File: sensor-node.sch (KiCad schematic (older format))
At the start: 38 parts

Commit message: init
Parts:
- U? (x2): symbol PS2811-1 -> PS2811-1-RESCUE-sensor-node
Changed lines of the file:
@@
 EESchema Schematic File Version 2
+LIBS:sensor-node-rescue
 LIBS:power
 LIBS:device
@@
 $EndComp
 $Comp
-L PS2811-1 U?
+L PS2811-1-RESCUE-sensor-node U?
 U 1 1 59702874
 P 2150 3600
@@
 $EndComp
 $Comp
-L PS2811-1 U?
+L PS2811-1-RESCUE-sensor-node U?
 U 1 1 59708087
 P 2150 4250

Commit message: init
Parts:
- removed J?: CONN_01X03, symbol CONN_01X03
- added J?: GND, symbol CONN_01X01
- added J?: +24, symbol CONN_01X01
- added J?: RJ45_B, symbol CONN_02X04
- added J?: ANALOG_IN, symbol CONN_01X02
- C? (x2): value C -> 0.1uF
- C?: value C -> 10uF
- C?: value C -> 4700pF
- C? (x2): value C -> 27pF
- C?: value CP -> 100uF
- C?: value CP -> 1000uF
- J?: value CONN_01X02 -> I2C
- J?: value OUTPUT -> DIGITAL_OUT
- J?: value INPUT -> DIGITAL_IN
- J?: value RJ45 -> RJ45_A
- R? (x2): value R -> 60
- R?: value R -> 300
- R? (x2): value R -> 4.7K
- Y?: value Crystal -> 8MHz
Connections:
- net +3V3: no longer J?.1 (P1), J?.2 (P2)
- net +5V: now also J?.1 (P1), J?.2 (P2), J?.1 (P1), J?.2 (P2)
- net CANH: now also J?.7 (P7), J?.7 (P7)
- net CANL: now also J?.8 (P8), J?.8 (P8)
- net GND: now also J?.5 (P5), J?.6 (P6), J?.1 (P1), J?.2 (P2), J?.5 (P5), J?.6 (P6); no longer J?.3 (P3), J?.4 (P4), U?.4 (D), U?.4 (D)
- net at U?.6 (PA0): now also J?.1 (P1)
- net at C?.2, R?.1, R?.1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: no longer J?.7 (P7), J?.8 (P8)
- net at J?.2 (P2), U?.2 (D): now also U?.4 (D)
- net at J?.1 (P1), U?.2 (D): now also U?.4 (D)
- new net +24V: J?.1 (P1), J?.3 (P3), J?.3 (P3), J?.4 (P4), J?.4 (P4)
- no-connect marks 2 -> 0
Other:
- moved on the sheet: J?

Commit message: updates
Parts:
- removed U?: LM1117-3.3, symbol LM1117-3.3
- added D3, D4: D_Schottky, Diodes_SMD:D_0805, symbol D_Schottky
- added D5: LED, Diodes_SMD:D_0805, symbol LED
- added J12: +5, ab2_connector:AB2_0.25_QD_TAB, symbol CONN_01X01
- added J8: CORTEX_DEBUG, Pin_Headers:Pin_Header_Straight_2x05_Pitch1.27mm, symbol CONN_02X05
- added R10: 250K, Resistors_SMD:R_0805_HandSoldering, symbol R
- added R16: 1K, Resistors_SMD:R_0805_HandSoldering, symbol R
- added R17: 330, Resistors_SMD:R_0805_HandSoldering, symbol R
- added R9: 7K, Resistors_SMD:R_0805_HandSoldering, symbol R
- added U1: LM1117-3.3, TO_SOT_Packages_SMD:SOT-223, symbol LM1117-3.3
- added U7: LM321, TO_SOT_Packages_SMD:SOT-23-5, symbol LM321
- C1: renamed from C?; value 100uF -> 10uF; footprint (none) -> Capacitors_SMD:C_0805_HandSoldering
- C2: renamed from C?; value 1000uF -> 100uF; footprint (none) -> Capacitors_SMD:C_1210_HandSoldering
- C3, C4, C5, C6, C7, C8: renamed from C?; footprint (none) -> Capacitors_SMD:C_0805_HandSoldering
- D1, D2: renamed from D?; footprint (none) -> Diodes_SMD:D_0805
- J1, J10, J11, J2: renamed from J?; footprint (none) -> Connectors_Terminal_Blocks:TerminalBlock_Pheonix_MKDS1.5-2pol
- J3, J4: renamed from J?; footprint (none) -> ab2_connector:AB2_0.25_QD_TAB
- J5, J6: renamed from J?; footprint (none) -> Pin_Headers:Pin_Header_Straight_1x02_Pitch2.54mm
- J7, J9: renamed from J?; footprint (none) -> Connectors:RJ45_8
- R1, R11, R12, R13, R14, R15, R2, R3, R4, R5, R6, R7, R8: renamed from R?; footprint (none) -> Resistors_SMD:R_0805_HandSoldering
- U2, U3: renamed from U?; footprint (none) -> Housings_SSOP:SOP-4_4.4x2.8mm_Pitch1.27mm
- U4: renamed from U?; footprint (none) -> Housings_QFP:LQFP-32_7x7mm_Pitch0.8mm
- U5, U6: renamed from U?; footprint (none) -> TO_SOT_Packages_SMD:SOT-223
- Y1: renamed from Y?; footprint (none) -> Crystals:Crystal_SMD_HC49-SD_HandSoldering
- gave numbers to parts that had none: 1
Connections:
- net +24V: now also U7.5 (V+)
- net +3V3: now also D3.1 (K), J8.1 (P1), U1.2 (VO), U1.4 (VO), U7.1 (+); no longer U4.4 (NRST)
- net +5V: now also J12.1 (P1), R17.2, U1.3 (VI)
- net GND: now also D4.2 (A), D5.1 (K), J8.3 (P3), J8.5 (P5), U1.1 (GND/ADJ), U7.2 (V-)
- net SWCLK: now also J8.4 (P4)
- net SWDIO: now also J8.2 (P2)
- net at U4.6 (PA0): now also D3.2 (A), D4.1 (K), R16.2; no longer J11.1 (P1)
- new net: J11.1 (P1), R10.1
- new net: R10.2, R9.1, U7.3 (-)
- new net: R16.1, R9.2, U7.4
- new net: D5.2 (A), R17.1
- new net NRST: J8.10 (P10), U4.4 (NRST)
- no-connect marks 0 -> 17

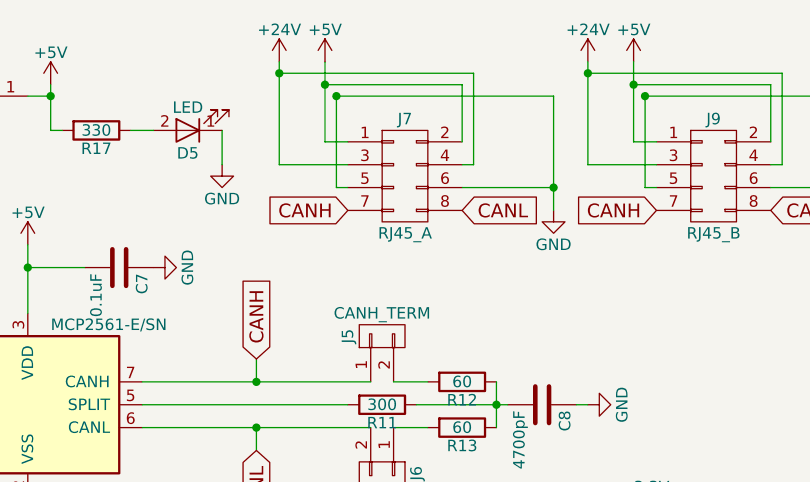
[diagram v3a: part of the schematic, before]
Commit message: Layout chaged for better routing on  the CAN differential
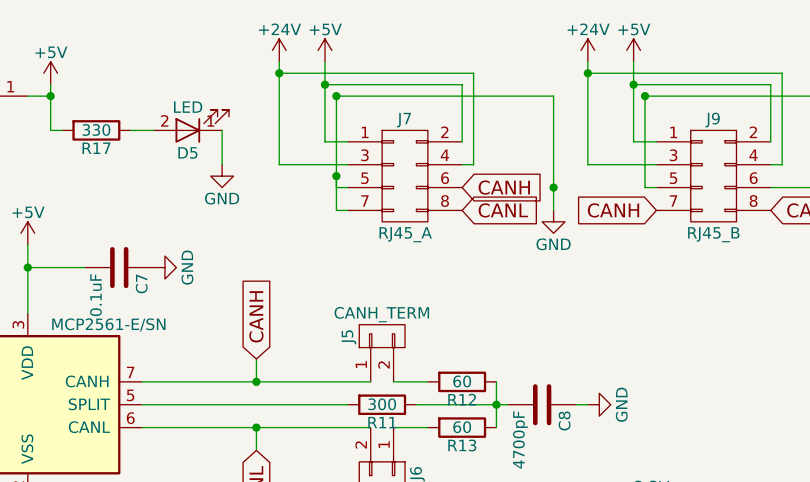
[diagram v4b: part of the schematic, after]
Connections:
- net CANH: now also J7.6 (P6); no longer J7.7 (P7)
- net GND: now also J7.7 (P7); no longer J7.6 (P6)
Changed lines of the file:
@@
 Text GLabel 8450 2000 1    60   Input ~ 0
 CANH
-Text GLabel 8850 1350 0    60   Input ~ 0
+Text GLabel 9350 1250 2    60   Input ~ 0
 CANH
 Text GLabel 9350 1350 2    60   Input ~ 0
@@
 Wire Wire Line
 	9750 1350 9750 850
-Wire Wire Line
-	9350 1250 9750 1250
 Connection ~ 9750 1250
 Wire Wire Line
@@
 Wire Wire Line
 	8300 1150 8300 1000
+Wire Wire Line
+	8850 1350 8800 1350
+Wire Wire Line
+	8800 1350 8800 1200
+Connection ~ 8800 1200
 $EndSCHEMATC

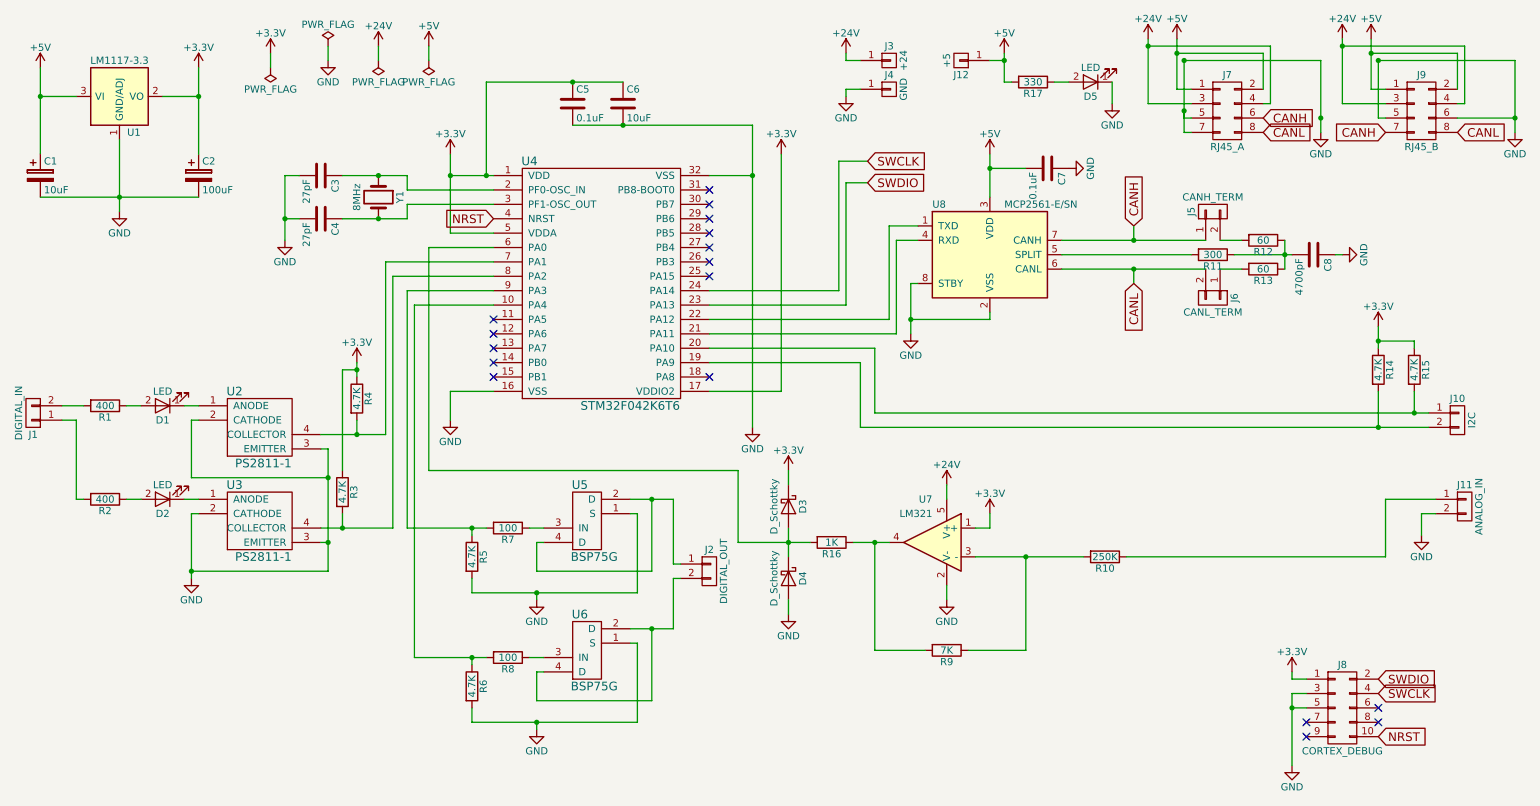
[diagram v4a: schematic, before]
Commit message: Adding voltage divider/unity gain analog front end
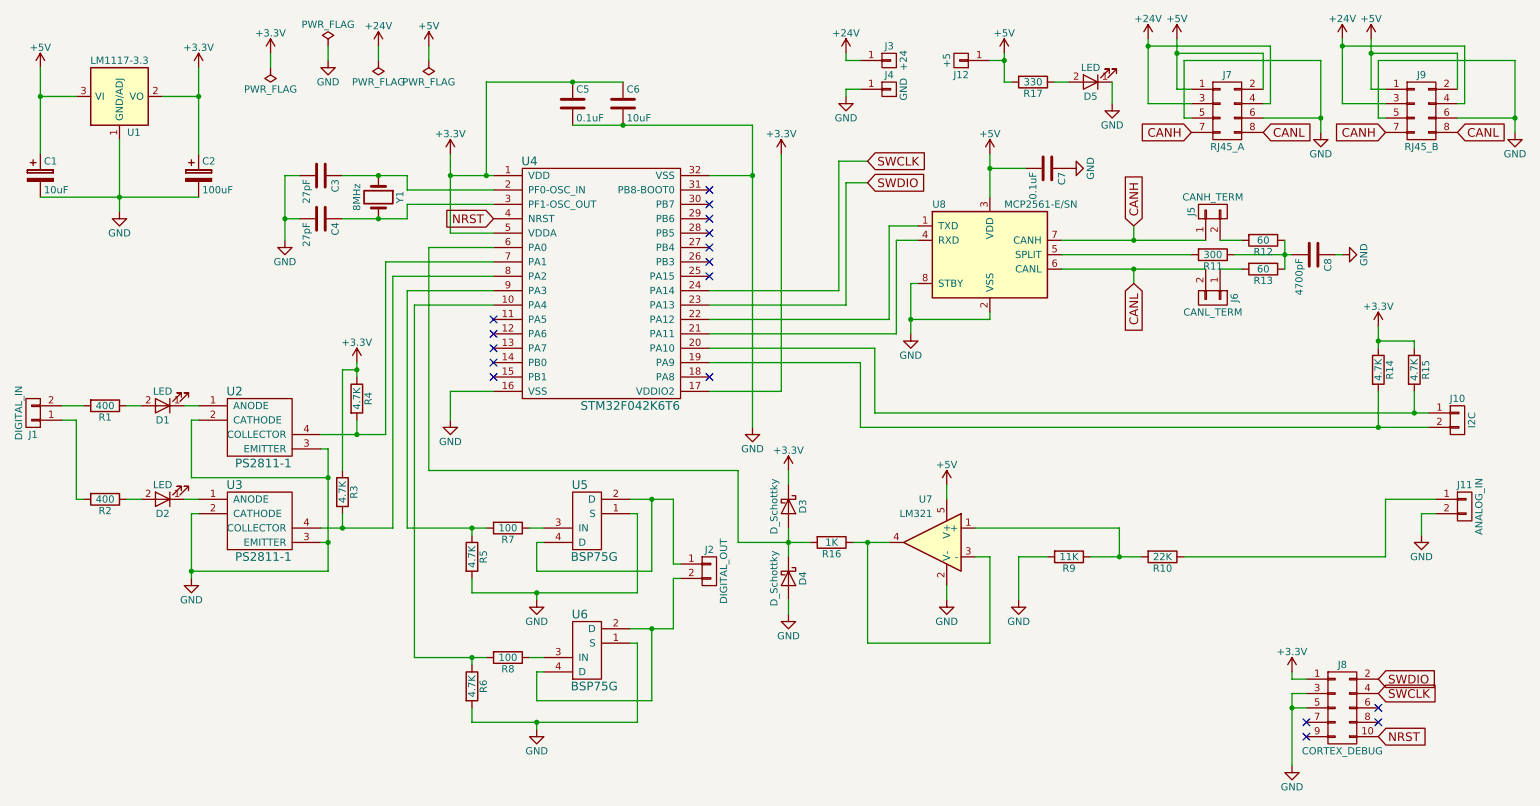
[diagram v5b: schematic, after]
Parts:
- R10: value 250K -> 22K
- R9: value 7K -> 11K
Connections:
- net +24V: no longer U7.5 (V+)
- net +3V3: no longer U7.1 (+)
- net +5V: now also U7.5 (V+)
- net CANH: now also J7.7 (P7); no longer J7.6 (P6)
- net GND: now also J7.6 (P6), R9.2; no longer J7.7 (P7)
- net at R10.2, R9.1: now also U7.1 (+); no longer U7.3 (-)
- net at R16.1, U7.4: now also U7.3 (-); no longer R9.2
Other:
- moved on the sheet: R10, R9
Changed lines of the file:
@@
 Text GLabel 8450 2000 1    60   Input ~ 0
 CANH
-Text GLabel 9350 1250 2    60   Input ~ 0
+Text GLabel 8850 1350 0    60   Input ~ 0
 CANH
 Text GLabel 9350 1350 2    60   Input ~ 0
@@
 Wire Wire Line
 	9750 1350 9750 850
-Connection ~ 9750 1250
 Wire Wire Line
 	8850 1250 8800 1250
 Wire Wire Line
 	8800 1250 8800 850
-Connection ~ 8800 850
 Wire Wire Line
 	8800 850  9750 850
@@
 Wire Wire Line
 	10150 1250 10150 850
-Connection ~ 10150 850
 Wire Wire Line
 	10150 850  11100 850
@@
 Wire Wire Line
 	7150 4600 7150 4500
-$Comp
-L +24V #PWR027
-U 1 1 59719679
-P 7150 3800
-F 0 "#PWR027" H 7150 3650 50  0001 C CNN
-F 1 "+24V" H 7150 3940 50  0000 C CNN
-F 2 "" H 7150 3800 50  0001 C CNN
-F 3 "" H 7150 3800 50  0001 C CNN
-	1    7150 3800
-	-1   0    0    -1
-$EndComp
 Wire Wire Line
 	7150 3800 7150 3900
-Wire Wire Line
-	7450 4100 7350 4100
 $Comp
 L R R9
 U 1 1 5971A94B
-P 7150 4950
-F 0 "R9" V 7230 4950 50  0000 C CNN
-F 1 "7K" V 7150 4950 50  0000 C CNN
-F 2 "Resistors_SMD:R_0805_HandSoldering" V 7080 4950 50  0001 C CNN
-F 3 "" H 7150 4950 50  0001 C CNN
-	1    7150 4950
+P 8000 4300
+F 0 "R9" V 8080 4300 50  0000 C CNN
+F 1 "11K" V 8000 4300 50  0000 C CNN
+F 2 "Resistors_SMD:R_0805_HandSoldering" V 7930 4300 50  0001 C CNN
+F 3 "" H 8000 4300 50  0001 C CNN
+	1    8000 4300
 	0    1    1    0
 $EndComp
 Wire Wire Line
-	7000 4950 6650 4950
-Wire Wire Line
-	6650 4950 6650 4200
-Connection ~ 6650 4200
-Wire Wire Line
 	10200 4300 10200 3900
 Wire Wire Line
 	10200 3900 10550 3900
-Wire Wire Line
-	7300 4950 7700 4950
-Wire Wire Line
-	7700 4950 7700 4300
-Connection ~ 7700 4300
 $Comp
 L R R10
 U 1 1 5971C15F
-P 8250 4300
-F 0 "R10" V 8330 4300 50  0000 C CNN
-F 1 "250K" V 8250 4300 50  0000 C CNN
-F 2 "Resistors_SMD:R_0805_HandSoldering" V 8180 4300 50  0001 C CNN
-F 3 "" H 8250 4300 50  0001 C CNN
-	1    8250 4300
+P 8650 4300
+F 0 "R10" V 8730 4300 50  0000 C CNN
+F 1 "22K" V 8650 4300 50  0000 C CNN
+F 2 "Resistors_SMD:R_0805_HandSoldering" V 8580 4300 50  0001 C CNN
+F 3 "" H 8650 4300 50  0001 C CNN
+	1    8650 4300
 	0    1    1    0
 $EndComp
-Wire Wire Line
-	7350 4300 8100 4300
-Wire Wire Line
-	8400 4300 10200 4300
 $Comp
 L CONN_02X05 J8
@@
 NoConn ~ 9650 5450
 $Comp
-L +3.3V #PWR028
+L +3.3V #PWR027
 U 1 1 59721CCA
 P 9550 5100
-F 0 "#PWR028" H 9550 4950 50  0001 C CNN
+F 0 "#PWR027" H 9550 4950 50  0001 C CNN
 F 1 "+3.3V" H 9550 5240 50  0000 C CNN
 F 2 "" H 9550 5100 50  0001 C CNN
@@
 	9550 5150 9550 5100
 $Comp
-L GND #PWR029
+L GND #PWR028
 U 1 1 59721E50
 P 9550 5750
-F 0 "#PWR029" H 9550 5500 50  0001 C CNN
+F 0 "#PWR028" H 9550 5500 50  0001 C CNN
 F 1 "GND" H 9550 5600 50  0000 C CNN
 F 2 "" H 9550 5750 50  0001 C CNN
@@
 NoConn ~ 4000 3050
 NoConn ~ 5500 3050
-$Comp
-L +3.3V #PWR030
-U 1 1 597B815C
-P 7450 4000
-F 0 "#PWR030" H 7450 3850 50  0001 C CNN
-F 1 "+3.3V" H 7450 4140 50  0000 C CNN
-F 2 "" H 7450 4000 50  0001 C CNN
-F 3 "" H 7450 4000 50  0001 C CNN
-	1    7450 4000
-	1    0    0    -1
-$EndComp
-Wire Wire Line
-	7450 4000 7450 4100
 Wire Wire Line
 	6900 2400 6900 2750
@@
 	6750 2000 6950 2000
 $Comp
-L +3.3V #PWR031
+L +3.3V #PWR029
 U 1 1 596D9277
 P 1950 900
-F 0 "#PWR031" H 1950 750 50  0001 C CNN
+F 0 "#PWR029" H 1950 750 50  0001 C CNN
 F 1 "+3.3V" H 1950 1040 50  0000 C CNN
 F 2 "" H 1950 900 50  0001 C CNN
@@
 $EndComp
 $Comp
-L PWR_FLAG #FLG032
+L PWR_FLAG #FLG030
 U 1 1 597C3662
 P 2450 900
-F 0 "#FLG032" H 2450 975 50  0001 C CNN
+F 0 "#FLG030" H 2450 975 50  0001 C CNN
 F 1 "PWR_FLAG" H 2450 1050 50  0000 C CNN
 F 2 "" H 2450 900 50  0001 C CNN
@@
 $EndComp
 $Comp
-L +3.3V #PWR033
+L +3.3V #PWR031
 U 1 1 597C372A
 P 2450 800
-F 0 "#PWR033" H 2450 650 50  0001 C CNN
+F 0 "#PWR031" H 2450 650 50  0001 C CNN
 F 1 "+3.3V" H 2450 940 50  0000 C CNN
 F 2 "" H 2450 800 50  0001 C CNN
@@
 	2450 900  2450 800
 $Comp
-L PWR_FLAG #FLG034
+L PWR_FLAG #FLG032
 U 1 1 597C4584
 P 2850 750
-F 0 "#FLG034" H 2850 825 50  0001 C CNN
+F 0 "#FLG032" H 2850 825 50  0001 C CNN
 F 1 "PWR_FLAG" H 2850 900 50  0000 C CNN
 F 2 "" H 2850 750 50  0001 C CNN
@@
 $EndComp
 $Comp
-L GND #PWR035
+L GND #PWR033
 U 1 1 597C45F2
 P 2850 850
-F 0 "#PWR035" H 2850 600 50  0001 C CNN
+F 0 "#PWR033" H 2850 600 50  0001 C CNN
 F 1 "GND" H 2850 700 50  0000 C CNN
 F 2 "" H 2850 850 50  0001 C CNN
@@
 	2850 850  2850 750
 $Comp
-L PWR_FLAG #FLG036
+L PWR_FLAG #FLG034
 U 1 1 597C6EB9
 P 3200 850
-F 0 "#FLG036" H 3200 925 50  0001 C CNN
+F 0 "#FLG034" H 3200 925 50  0001 C CNN
 F 1 "PWR_FLAG" H 3200 1000 50  0000 C CNN
 F 2 "" H 3200 850 50  0001 C CNN
@@
 $EndComp
 $Comp
-L +24V #PWR037
+L +24V #PWR035
 U 1 1 597C6F27
 P 3200 750
-F 0 "#PWR037" H 3200 600 50  0001 C CNN
+F 0 "#PWR035" H 3200 600 50  0001 C CNN
 F 1 "+24V" H 3200 890 50  0000 C CNN
 F 2 "" H 3200 750 50  0001 C CNN
@@
 	3200 750  3200 850
 $Comp
-L +5V #PWR038
+L +5V #PWR036
 U 1 1 597C81E6
 P 3550 750
-F 0 "#PWR038" H 3550 600 50  0001 C CNN
+F 0 "#PWR036" H 3550 600 50  0001 C CNN
 F 1 "+5V" H 3550 890 50  0000 C CNN
 F 2 "" H 3550 750 50  0001 C CNN
@@
 $EndComp
 $Comp
-L PWR_FLAG #FLG039
+L PWR_FLAG #FLG037
 U 1 1 597C82AE
 P 3550 850
-F 0 "#FLG039" H 3550 925 50  0001 C CNN
+F 0 "#FLG037" H 3550 925 50  0001 C CNN
 F 1 "PWR_FLAG" H 3550 1000 50  0000 C CNN
 F 2 "" H 3550 850 50  0001 C CNN
@@
 $EndComp
 $Comp
-L +5V #PWR040
+L +5V #PWR038
 U 1 1 597AB996
 P 7550 800
-F 0 "#PWR040" H 7550 650 50  0001 C CNN
+F 0 "#PWR038" H 7550 650 50  0001 C CNN
 F 1 "+5V" H 7550 940 50  0000 C CNN
 F 2 "" H 7550 800 50  0001 C CNN
@@
 	5700 3700 3550 3700
 $Comp
-L GND #PWR041
+L GND #PWR039
 U 1 1 597BFE51
 P 6050 4700
-F 0 "#PWR041" H 6050 4450 50  0001 C CNN
+F 0 "#PWR039" H 6050 4450 50  0001 C CNN
 F 1 "GND" H 6050 4550 50  0000 C CNN
 F 2 "" H 6050 4700 50  0001 C CNN
@@
 	6050 4700 6050 4600
 $Comp
-L +3.3V #PWR042
+L +3.3V #PWR040
 U 1 1 597C041B
 P 6050 3700
-F 0 "#PWR042" H 6050 3550 50  0001 C CNN
+F 0 "#PWR040" H 6050 3550 50  0001 C CNN
 F 1 "+3.3V" H 6050 3840 50  0000 C CNN
 F 2 "" H 6050 3700 50  0001 C CNN
@@
 Connection ~ 7550 850
 $Comp
-L GND #PWR043
+L GND #PWR041
 U 1 1 597CDFFA
 P 8300 1150
-F 0 "#PWR043" H 8300 900 50  0001 C CNN
+F 0 "#PWR041" H 8300 900 50  0001 C CNN
 F 1 "GND" H 8300 1000 50  0000 C CNN
 F 2 "" H 8300 1150 50  0001 C CNN
@@
 	8300 1150 8300 1000
 Wire Wire Line
-	8850 1350 8800 1350
-Wire Wire Line
-	8800 1350 8800 1200
-Connection ~ 8800 1200
+	7350 4300 7450 4300
+Wire Wire Line
+	7450 4300 7450 4900
+Wire Wire Line
+	7450 4900 6600 4900
+Wire Wire Line
+	6600 4900 6600 4200
+Connection ~ 6600 4200
+$Comp
+L +5V #PWR042
+U 1 1 597FBC2C
+P 7150 3800
+F 0 "#PWR042" H 7150 3650 50  0001 C CNN
+F 1 "+5V" H 7150 3940 50  0000 C CNN
+F 2 "" H 7150 3800 50  0001 C CNN
+F 3 "" H 7150 3800 50  0001 C CNN
+	1    7150 3800
+	1    0    0    -1
+$EndComp
+Wire Wire Line
+	7850 4300 7650 4300
+$Comp
+L GND #PWR043
+U 1 1 597FBE67
+P 7650 4600
+F 0 "#PWR043" H 7650 4350 50  0001 C CNN
+F 1 "GND" H 7650 4450 50  0000 C CNN
+F 2 "" H 7650 4600 50  0001 C CNN
+F 3 "" H 7650 4600 50  0001 C CNN
+	1    7650 4600
+	1    0    0    -1
+$EndComp
+Wire Wire Line
+	7650 4300 7650 4600
+Wire Wire Line
+	8150 4300 8500 4300
+Wire Wire Line
+	8800 4300 10200 4300
+Wire Wire Line
+	8350 4300 8350 4100
+Wire Wire Line
+	8350 4100 7350 4100
+Connection ~ 8350 4300
+Wire Wire Line
+	9350 1250 9750 1250
+Connection ~ 9750 1250
 $EndSCHEMATC
